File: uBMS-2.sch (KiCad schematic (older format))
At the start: 66 parts, among them Q1 NTD5865NL, Q2 2N7002, Q3 2N7002, U1 ESP32-WROOM-32, U10 VDMG10C0, U2 TLV1117-33, U3 LM2576HVS-5, U4 MCP23017_SS, U5 TL431DBV, U6 TSC2012IDT, U7 ADS1115IDGS, U8 MCP23017_SS, U9 MCP23017_SS

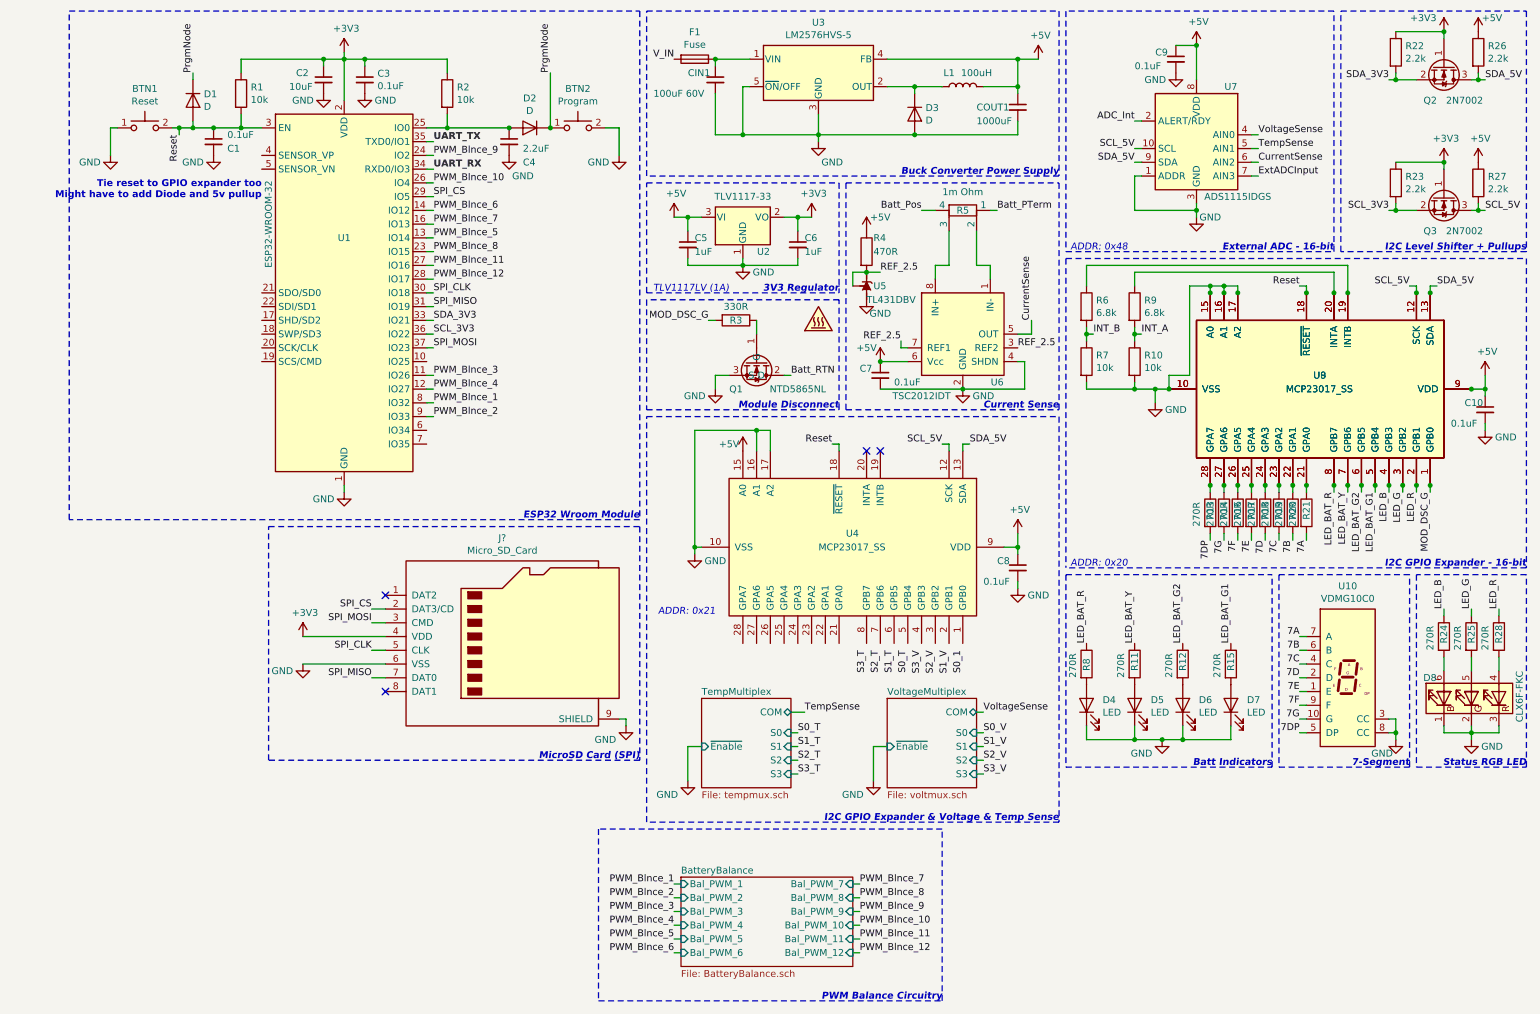
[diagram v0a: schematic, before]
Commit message: Fixed pull up for enable pin on GPIO
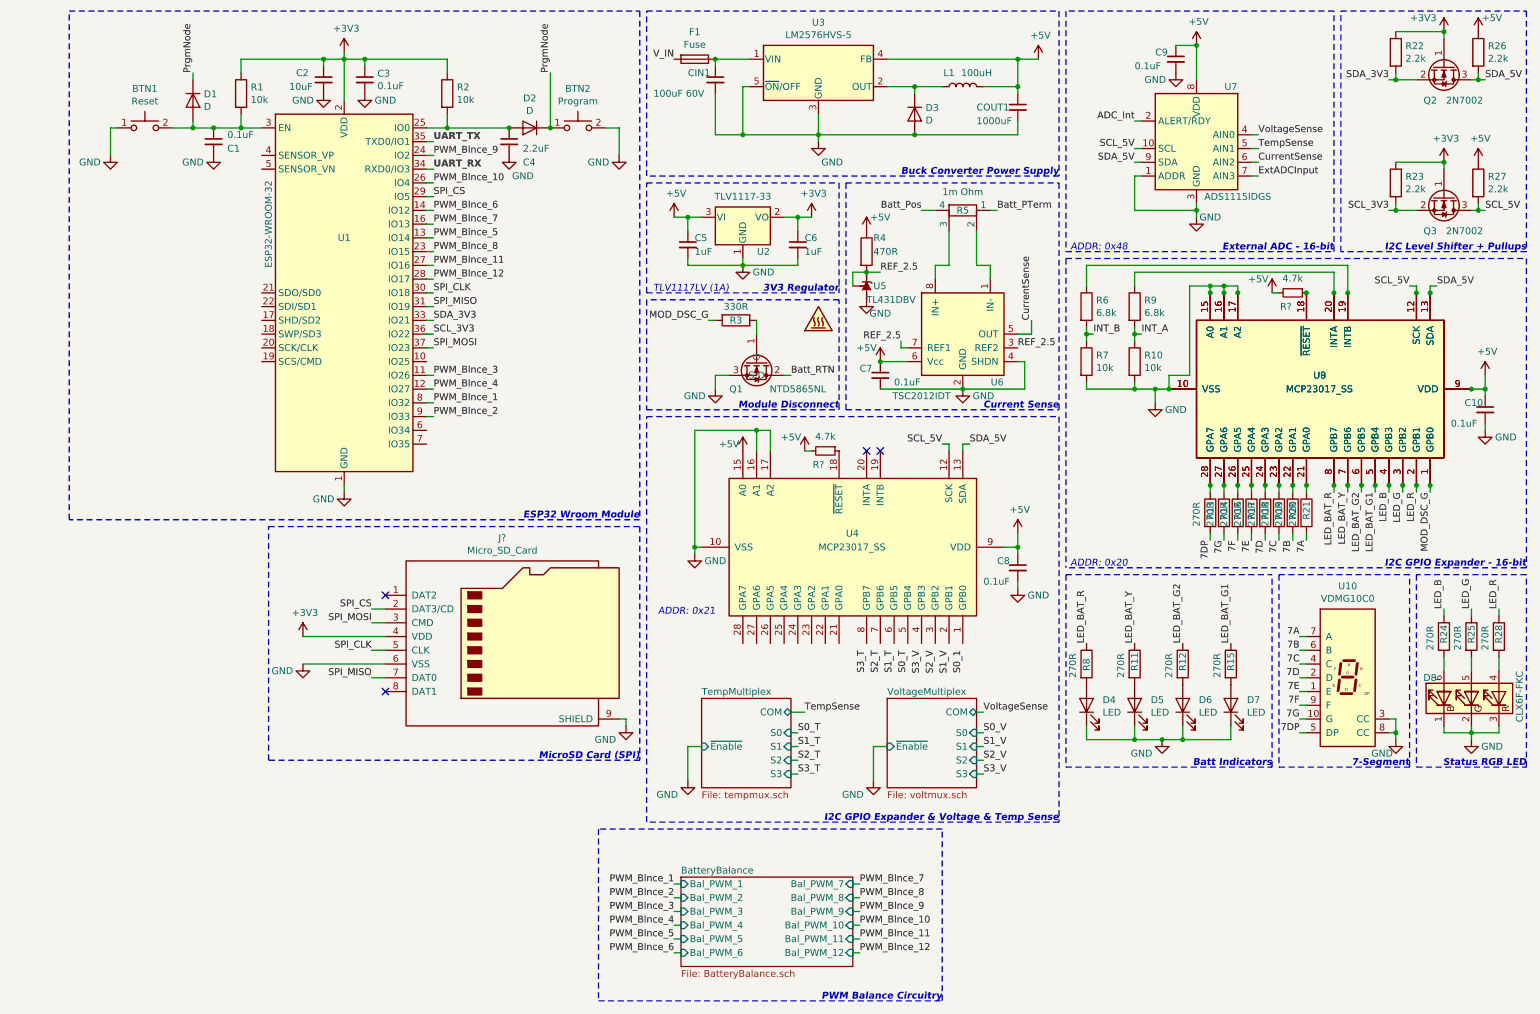
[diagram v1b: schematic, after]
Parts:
- added R? (x2): 4.7k, symbol Device:R_Small
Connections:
- net +5V: now also R?.2, R?.2
- net Reset: no longer names the net of BTN1.2, C1.1, D1.2 (A), R1.2, U1.3 (EN)
- net Reset: no longer U4.18 (~RESET~), U8.18 (~RESET~), U9.18 (~RESET~)
- new net: R?.1, U8.18 (~RESET~), U9.18 (~RESET~)
- new net: R?.1, U4.18 (~RESET~)
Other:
- note removed: "Tie reset to GPIO expander too\nMight have to add Diode and 5v pullup\n\n"
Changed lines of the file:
@@
 Wire Wire Line
 	850  1400 900  1400
-Wire Wire Line
-	1300 1400 1350 1400
 $Comp
 L Device:R R2
@@
 	1    0    0    -1
 $EndComp
-Text Notes 1950 2000 2    50   ~ 10
-Tie reset to GPIO expander too\nMight have to add Diode and 5v pullup\n\n
 $Comp
 L uBMS-Parts:CLX6F-FKC D8
@@
 NoConn ~ 6350 3750
 NoConn ~ 6450 3750
-Text Label 1350 1450 3    50   ~ 0
-Reset
-Wire Wire Line
-	1350 1450 1350 1400
-Connection ~ 1350 1400
-Wire Wire Line
-	1350 1400 1450 1400
-Text Label 9500 2550 2    50   ~ 0
-Reset
-Text Label 6100 3700 2    50   ~ 0
-Reset
-Wire Wire Line
-	6150 3750 6150 3700
-Wire Wire Line
-	6150 3700 6100 3700
-Wire Wire Line
-	9550 2600 9550 2550
-Wire Wire Line
-	9550 2550 9500 2550
-Connection ~ 9550 2600
 Text Notes 5250 4950 2    50   Italic 0
 ADDR: 0x21
@@
 Text Notes 4700 6000 2    50   Italic 10
 MicroSD Card (SPI)
+Wire Wire Line
+	1300 1400 1450 1400
+$Comp
+L Device:R_Small R?
+U 1 1 5F3904DB
+P 6050 3750
+F 0 "R?" V 6150 3700 50  0000 C CNN
+F 1 "4.7k" V 5945 3750 50  0000 C CNN
+F 2 "" H 6050 3750 50  0001 C CNN
+F 3 "~" H 6050 3750 50  0001 C CNN
+	1    6050 3750
+	0    1    1    0
+$EndComp
+$Comp
+L Device:R_Small R?
+U 1 1 5F391C37
+P 9450 2600
+F 0 "R?" V 9550 2550 50  0000 C CNN
+F 1 "4.7k" V 9345 2600 50  0000 C CNN
+F 2 "" H 9450 2600 50  0001 C CNN
+F 3 "~" H 9450 2600 50  0001 C CNN
+	1    9450 2600
+	0    1    1    0
+$EndComp
+Connection ~ 9550 2600
+$Comp
+L power:+5V #PWR?
+U 1 1 5F39226C
+P 5900 3750
+F 0 "#PWR?" H 5900 3600 50  0001 C CNN
+F 1 "+5V" H 5800 3850 50  0000 C CNN
+F 2 "" H 5900 3750 50  0001 C CNN
+F 3 "" H 5900 3750 50  0001 C CNN
+	1    5900 3750
+	1    0    0    -1
+$EndComp
+Wire Wire Line
+	5950 3750 5900 3750
+$Comp
+L power:+5V #PWR?
+U 1 1 5F3A8B61
+P 9300 2600
+F 0 "#PWR?" H 9300 2450 50  0001 C CNN
+F 1 "+5V" H 9200 2700 50  0000 C CNN
+F 2 "" H 9300 2600 50  0001 C CNN
+F 3 "" H 9300 2600 50  0001 C CNN
+	1    9300 2600
+	1    0    0    -1
+$EndComp
+Wire Wire Line
+	9300 2600 9350 2600
 $EndSCHEMATC

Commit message: Added buttons + redid numbering
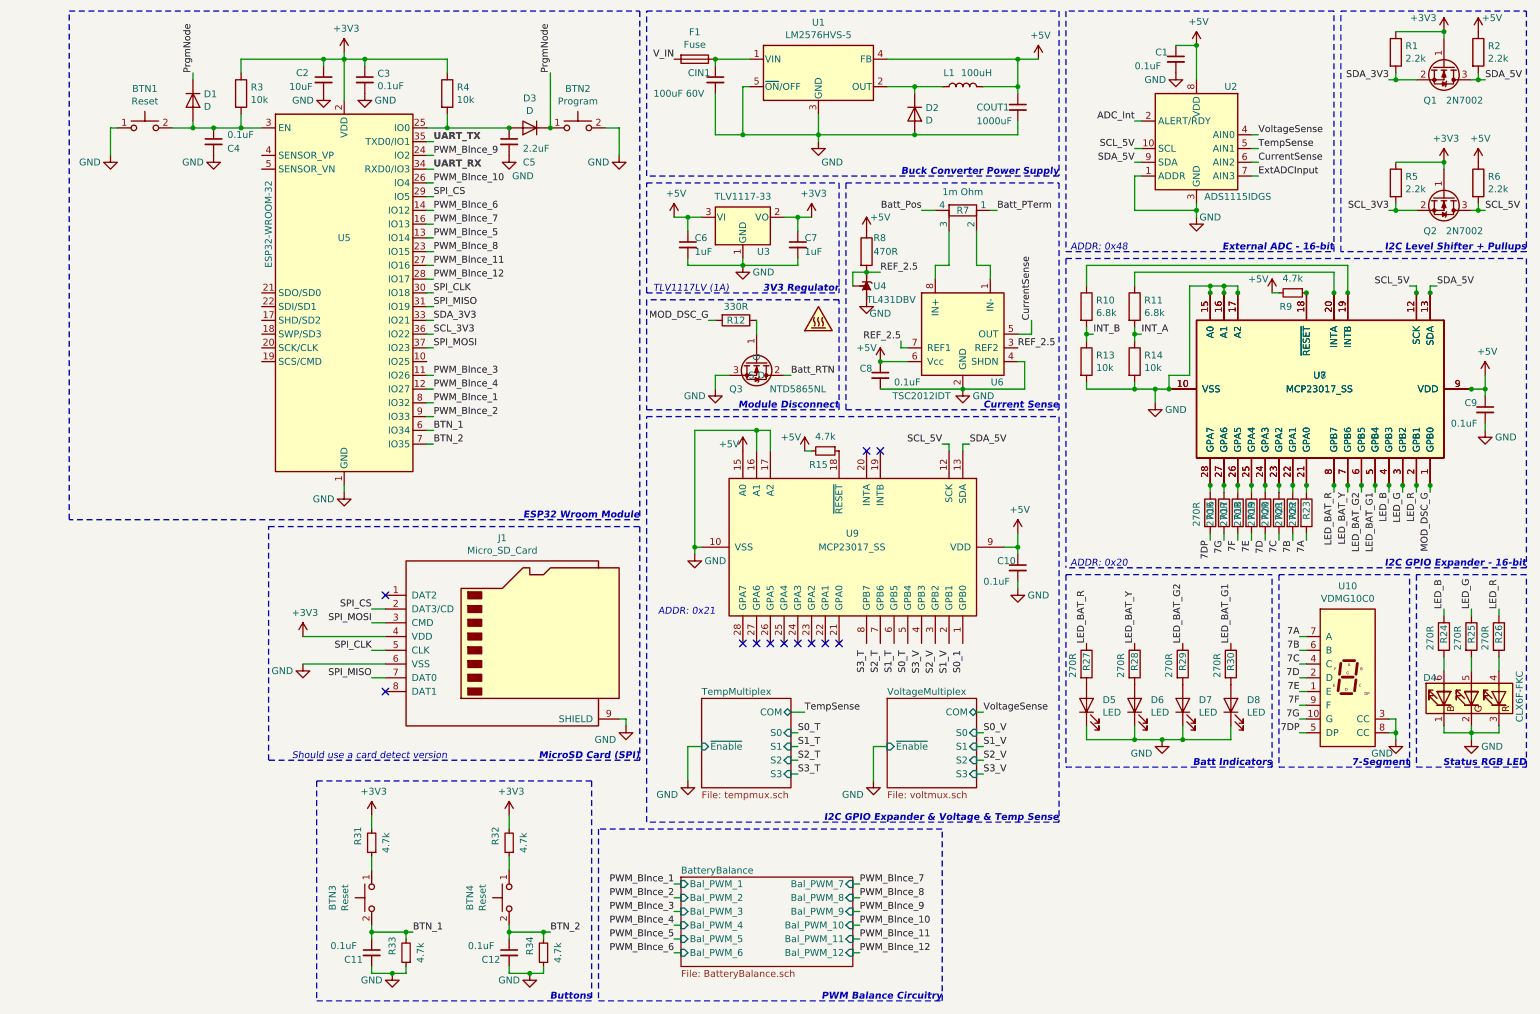
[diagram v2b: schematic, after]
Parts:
- added BTN3, BTN4: Reset, Lafayette_Electric_Car_Footprints:PushButton, symbol Lafayette_Electric_Car_Internals:PushButton
- added C11, C12: 0.1uF, symbol Device:C_Small
- added R31, R32, R33, R34: 4.7k, symbol Device:R_Small
- gave numbers to parts that had none: 3
- renumbered C9 to C1, C8 to C10, C1 to C4, C4 to C5, C5 to C6, C6 to C7, C7 to C8, C10 to C9, D3 to D2, D2 to D3, D8 to D4, D4 to D5, D5 to D6, D6 to D7, D7 to D8, Q2 to Q1, Q3 to Q2, Q1 to Q3, R22 to R1, R6 to R10, R9 to R11, R3 to R12, R7 to R13, R10 to R14, R13 to R16, R14 to R17, R16 to R18, R17 to R19, R26 to R2, R18 to R20, R19 to R21, R20 to R22, R21 to R23, R28 to R26, R8 to R27, R11 to R28, R12 to R29, R1 to R3, R15 to R30, R2 to R4, R23 to R5, R27 to R6, R5 to R7, R4 to R8, U3 to U1, U7 to U2, U2 to U3, U5 to U4, U1 to U5, U8 to U7, U9 to U8, U4 to U9
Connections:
- net +3V3: now also R31.2, R32.2
- net GND: now also C11.2, C12.2, R33.1, R34.1
- net BTN_1: now reaches U5.6 (IO34)
- net BTN_1: now also BTN3.2, C11.1, R33.2
- net BTN_2: now reaches U5.7 (IO35)
- net BTN_2: now also BTN4.2, C12.1, R34.2
- new net: BTN3.1, R31.1
- new net: BTN4.1, R32.1
- no-connect marks 4 -> 12
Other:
- note added: "Buttons"
- note added: "Should use a card detect version"

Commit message: Added PCB temp sensors and redit numberings
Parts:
- BTN1: footprint Lafayette_Electric_Car_Footprints:PushButton -> (none)
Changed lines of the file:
@@
 F 0 "BTN1" H 1100 1685 50  0000 C CNN
 F 1 "Reset" H 1100 1594 50  0000 C CNN
-F 2 "Lafayette_Electric_Car_Footprints:PushButton" H 1350 1600 50  0001 C CNN
+F 2 "" H 1350 1600 50  0001 C CNN
 F 3 "https://media.digikey.com/pdf/Data%20Sheets/RAFI%20PDF's/Racon_PCB_Tactile_Switches_Cat.pdf" H 1350 1600 50  0001 C CNN
 F 4 "Digikey" H 900 1750 50  0001 C CNN "Vendor"

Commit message: Added most footprints
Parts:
- removed U8: MCP23017_SS, Package_SO:SSOP-28_5.3x10.2mm_P0.65mm, symbol Interface_Expansion:MCP23017_SS
- BTN1: footprint (none) -> Button_Switch_SMD:PTS636_SM43_SMTR_LFS_6mm_3,5mm
- BTN2: footprint Lafayette_Electric_Car_Footprints:PushButton -> Button_Switch_SMD:PTS636_SM43_SMTR_LFS_6mm_3,5mm
- BTN3: value Reset -> Input_1; footprint Lafayette_Electric_Car_Footprints:PushButton -> Button_Switch_SMD:PTS636_SM43_SMTR_LFS_6mm_3,5mm
- BTN4: value Reset -> Input_2; footprint Lafayette_Electric_Car_Footprints:PushButton -> Button_Switch_SMD:PTS636_SM43_SMTR_LFS_6mm_3,5mm
- C1, C10, C11, C12, C2, C3, C4, C5, C6, C7, C8, C9: footprint (none) -> Capacitor_SMD:C_1206_3216Metric
- CIN1, COUT1: footprint (none) -> Capacitor_SMD:CP_Elec_10x10
- D1, D2, D3: footprint (none) -> Diode_SMD:D_0603_1608Metric_Pad1.05x0.95mm_HandSolder
- D5, D6, D7, D8: footprint (none) -> LED_SMD:LED_1206_3216Metric_Pad1.42x1.75mm_HandSolder
- F1: value Fuse -> 1A PTC; footprint (none) -> Fuse:Fuse_2920_7451Metric_Pad2.10x5.45mm_HandSolder
- L1: footprint (none) -> Inductor_SMD:L_12x12mm_H8mm
- R1, R10, R11, R12, R13, R14, R15, R16, R17, R18, R19, R2, R20, R21, R22, R23, R24, R25, R26, R27, R28, R29, R3, R30, R31, R32, R33, R34, R4, R5, R6, R8, R9: footprint (none) -> Resistor_SMD:R_0603_1608Metric_Pad1.05x0.95mm_HandSolder
- U3: footprint (none) -> Package_TO_SOT_SMD:SOT-223-3_TabPin2
- renumbered U9 to U8, U10 to U9
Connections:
- net S0_1: now also U8.1 (GPB0)
- net S0_T: now also U8.5 (GPB4)
- net S1_T: now also U8.6 (GPB5)
- net S1_V: now also U8.2 (GPB1)
- net S2_T: now also U8.7 (GPB6)
- net S2_V: now also U8.3 (GPB2)
- net S3_T: now also U8.8 (GPB7)
- net S3_V: now also U8.4 (GPB3)

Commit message: added card detect sd card stuff
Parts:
- removed J1: Micro_SD_Card, symbol Connector:Micro_SD_Card
- added J1: Micro_SD_Card_Det, symbol Connector:Micro_SD_Card_Det
- added R92: 4.7k, Resistor_SMD:R_0603_1608Metric_Pad1.05x0.95mm_HandSolder, symbol Device:R_Small
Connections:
- net +3V3: now also J1.4 (VDD), R92.2
- net GND: now also J1.11 (SHIELD), J1.6 (VSS)
- net SPI_CLK: now also J1.5 (CLK)
- net SPI_CS: now also J1.2 (DAT3/CD)
- net SPI_MISO: now also J1.7 (DAT0)
- net SPI_MOSI: now also J1.3 (CMD)
- net SD_Detect: now reaches U5.10 (IO25)
- net SD_Detect: now also J1.10 (DET_A), R92.1
- no-connect marks 12 -> 13
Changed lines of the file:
@@
 	4750 2600 6150 2600
-$Comp
-L Connector:Micro_SD_Card J1
-U 1 1 5F239FEE
-P 3750 5100
-F 0 "J1" H 3700 5817 50  0000 C CNN
-F 1 "Micro_SD_Card" H 3700 5726 50  0000 C CNN
-F 2 "" H 4900 5400 50  0001 C CNN
-F 3 "http://katalog.we-online.de/em/datasheet/693072010801.pdf" H 3750 5100 50  0001 C CNN
-	1    3750 5100
-	1    0    0    -1
-$EndComp
 $Comp
 L power:GND #PWR037
@@
 P 4600 5750
 F 0 "#PWR037" H 4600 5500 50  0001 C CNN
-F 1 "GND" H 4450 5650 50  0000 C CNN
+F 1 "GND" H 4500 5750 50  0000 C CNN
 F 2 "" H 4600 5750 50  0001 C CNN
 F 3 "" H 4600 5750 50  0001 C CNN
@@
 Wire Wire Line
 	6350 5200 6350 5150
+$Comp
+L Connector:Micro_SD_Card_Det J1
+U 1 1 5F28F4CE
+P 3750 5200
+F 0 "J1" H 3700 6017 50  0000 C CNN
+F 1 "Micro_SD_Card_Det" H 3700 5926 50  0000 C CNN
+F 2 "" H 5800 5900 50  0001 C CNN
+F 3 "https://www.hirose.com/product/en/download_file/key_name/DM3/category/Catalog/doc_file_id/49662/?file_category_id=4&item_id=195&is_series=1" H 3750 5300 50  0001 C CNN
+	1    3750 5200
+	1    0    0    -1
+$EndComp
+NoConn ~ 2850 5700
+$Comp
+L Device:R_Small R92
+U 1 1 5F2E72B5
+P 3800 2900
+F 0 "R92" V 3900 2850 50  0000 C CNN
+F 1 "4.7k" V 3695 2900 50  0000 C CNN
+F 2 "Resistor_SMD:R_0603_1608Metric_Pad1.05x0.95mm_HandSolder" H 3800 2900 50  0001 C CNN
+F 3 "~" H 3800 2900 50  0001 C CNN
+	1    3800 2900
+	-1   0    0    1
+$EndComp
+$Comp
+L power:+3V3 #PWR089
+U 1 1 5F2E7B0B
+P 3800 2800
+F 0 "#PWR089" H 3800 2650 50  0001 C CNN
+F 1 "+3V3" H 3815 2973 50  0000 C CNN
+F 2 "" H 3800 2800 50  0001 C CNN
+F 3 "" H 3800 2800 50  0001 C CNN
+	1    3800 2800
+	1    0    0    -1
+$EndComp
+Text Label 3850 3100 0    50   ~ 0
+SD_Detect
+Wire Wire Line
+	3850 3100 3800 3100
+Wire Wire Line
+	3800 3000 3800 3100
+Connection ~ 3800 3100
+Wire Wire Line
+	3800 3100 3150 3100
+Text Label 2750 5600 2    50   ~ 0
+SD_Detect
+Wire Wire Line
+	2750 5600 2850 5600
 $EndSCHEMATC

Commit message: Switched to lower GPIO pin part to save space
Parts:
- removed R10, R11: 6.8k, Resistor_SMD:R_0603_1608Metric_Pad1.05x0.95mm_HandSolder, symbol Device:R
- removed R13, R14: 10k, Resistor_SMD:R_0603_1608Metric_Pad1.05x0.95mm_HandSolder, symbol Device:R
- removed R15: 4.7k, Resistor_SMD:R_0603_1608Metric_Pad1.05x0.95mm_HandSolder, symbol Device:R_Small
- removed U8: MCP23017_SS, Package_SO:SSOP-28_5.3x10.2mm_P0.65mm, symbol Interface_Expansion:MCP23017_SS
- added R20: 4.7k, Resistor_SMD:R_0603_1608Metric_Pad1.05x0.95mm_HandSolder, symbol Device:R_Small
- added U8: MCP23008-E_P, digikey-footprints:DIP-18_W7.62mm, symbol dk_Interface-I-O-Expanders:MCP23008-E_P
- renumbered R12 to R10, R92 to R11, R16 to R12, R17 to R13, R18 to R14, R19 to R15, R20 to R16, R21 to R17, R22 to R18, R23 to R19, R24 to R21, R25 to R22, R26 to R23, R27 to R24, R28 to R25, R29 to R26, R30 to R27, R31 to R28, R32 to R29, R33 to R30, R34 to R31
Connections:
- net +5V: now also R20.2, U8.9 (VSS)
- net GND: now also U8.18 (VDD), U8.3 (A2), U8.4 (A1)
- net S0_1: now also U8.10 (GP0)
- net S0_T: now also U8.14 (GP4)
- net S1_T: now also U8.15 (GP5)
- net S1_V: now also U8.11 (GP1)
- net S2_T: now also U8.16 (GP6)
- net S2_V: now also U8.12 (GP2)
- net S3_T: now also U8.17 (GP7)
- net S3_V: now also U8.13 (GP3)
- net SCL_5V: now also U8.1 (SCL)
- net SDA_5V: now also U8.2 (SDA)
- new net: R20.1, U8.5 (A0), U8.6 (~RESET)
- no-connect marks 13 -> 12
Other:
- moved on the sheet: C10, C9, R12, R13, R14, R15, R16, R17, R18, R19, R9, U7

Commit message: Created 7-seg footprint (local)
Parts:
- U8: footprint digikey-footprints:DIP-18_W7.62mm -> Package_SO:SOIC-18W_7.5x11.6mm_P1.27mm
- U9: footprint (none) -> Display_7Segment:VDMG10C0
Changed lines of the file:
@@
 F 0 "U9" H 9850 6067 50  0000 C CNN
 F 1 "VDMG10C0" H 9850 5976 50  0000 C CNN
-F 2 "" H 9850 5400 50  0001 C CNN
+F 2 "Display_7Segment:VDMG10C0" H 9850 5400 50  0001 C CNN
 F 3 "https://www.vishay.com/docs/84196/vdmx10x0.pdf" H 9850 5400 50  0001 C CNN
 	1    9850 5400
@@
 F 0 "U8" V 6000 4050 60  0000 R CNN
 F 1 "MCP23008-E_P" V 6300 4150 60  0000 R CNN
-F 2 "digikey-footprints:DIP-18_W7.62mm" H 6250 4350 60  0001 L CNN
+F 2 "Package_SO:SOIC-18W_7.5x11.6mm_P1.27mm" H 6250 4350 60  0001 L CNN
 F 3 "http://www.microchip.com/mymicrochip/filehandler.aspx?ddocname=en021920" H 6250 4450 60  0001 L CNN
 F 4 "MCP23008-E/P-ND" H 6250 4550 60  0001 L CNN "Digi-Key_PN"
